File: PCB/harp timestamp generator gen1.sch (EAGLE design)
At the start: 11 parts, among them IC1 ATXMEGAxxxA4U-AU

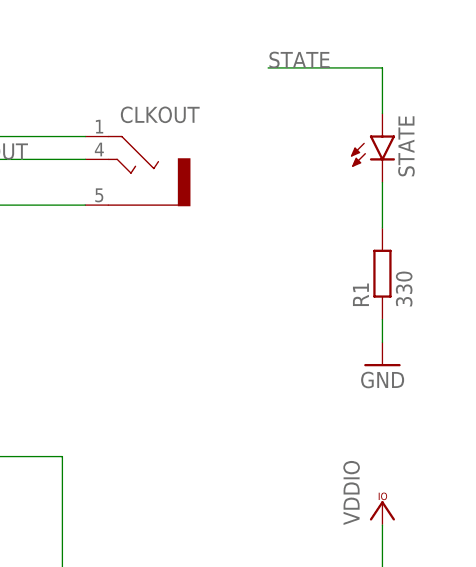
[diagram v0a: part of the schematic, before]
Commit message: Updated R1 to 910 ohms.
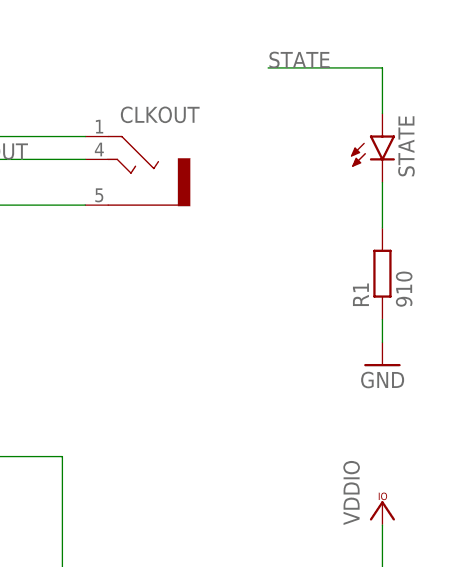
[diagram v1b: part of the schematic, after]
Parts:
- R1: value 330 -> 910
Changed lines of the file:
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@@
 <part name="VCC1" library="supply1" deviceset="VCCIO" device="" value="VDDIO"/>
 <part name="STATE" library="led" library_urn="urn:adsk.eagle:library:259" deviceset="LED" device="CHIP-LED0603" package3d_urn="urn:adsk.eagle:package:15819/3"/>
-<part name="R1" library="rcl" library_urn="urn:adsk.eagle:library:334" deviceset="R-EU_" device="R0402" package3d_urn="urn:adsk.eagle:package:23547/3" value="330"/>
+<part name="R1" library="rcl" library_urn="urn:adsk.eagle:library:334" deviceset="R-EU_" device="R0402" package3d_urn="urn:adsk.eagle:package:23547/3" value="910"/>
 <part name="GND1" library="supply1" deviceset="GND" device=""/>
 <part name="VCC2" library="supply1" deviceset="VCCIO" device="" value="VDDIO"/>

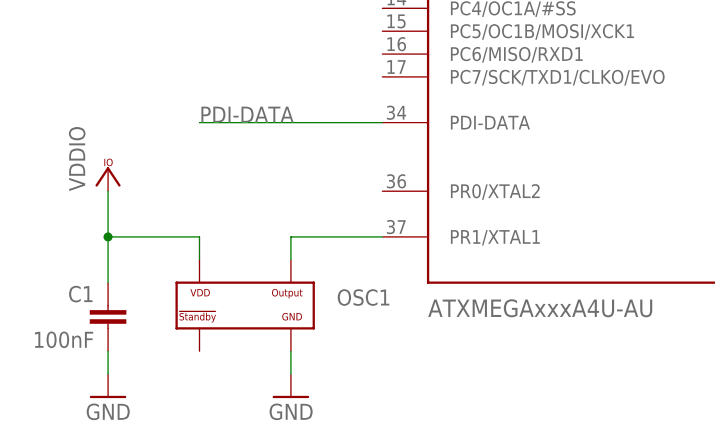
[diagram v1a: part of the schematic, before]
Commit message: Re-designed oscillator footprint for easier manual assembly
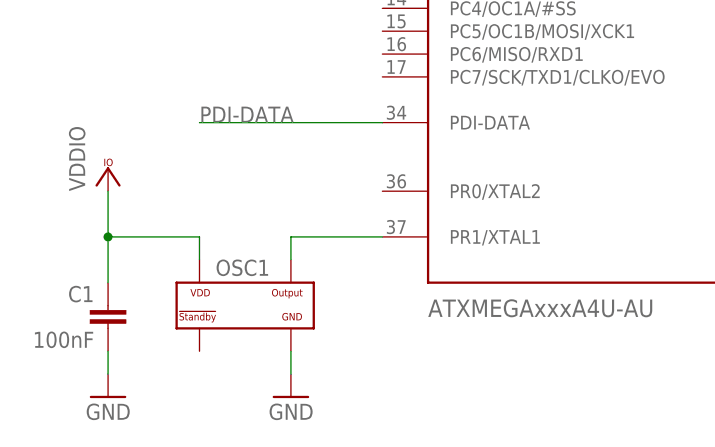
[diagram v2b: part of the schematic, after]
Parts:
- OSC1: value OSCILLATOR -> CNP-MISCELLANEOUS_OSCILLATOR; device CNP-miscellaneous:OSCILLATOR -> harp rfid reader v1.0:CNP-MISCELLANEOUS_OSCILLATOR
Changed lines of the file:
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@@
 <layer number="59" name="tCarbon" color="7" fill="1" visible="no" active="no"/>
 <layer number="60" name="bCarbon" color="7" fill="1" visible="no" active="no"/>
+<layer number="88" name="SimResults" color="9" fill="1" visible="yes" active="yes"/>
+<layer number="89" name="SimProbes" color="9" fill="1" visible="yes" active="yes"/>
 <layer number="90" name="Modules" color="7" fill="1" visible="yes" active="yes"/>
 <layer number="91" name="Nets" color="2" fill="1" visible="yes" active="yes"/>
@@
 <part name="VCC6" library="supply1" deviceset="VCCIO" device="" value="VDDIO"/>
 <part name="FRAME4" library="frames" deviceset="A3L-LOC" device=""/>
-<part name="OSC1" library="CNP-miscellaneous" deviceset="OSCILLATOR" device="" value=""/>
 <part name="GND59" library="supply1" deviceset="GND" device=""/>
 <part name="C1" library="rcl" deviceset="C-EU" device="C0402" value="100nF"/>
@@
 <part name="GND1" library="supply1" deviceset="GND" device=""/>
 <part name="VCC2" library="supply1" deviceset="VCCIO" device="" value="VDDIO"/>
+<part name="OSC1" library="harp rfid reader v1.0" deviceset="CNP-MISCELLANEOUS_OSCILLATOR" device=""/>
 </parts>
 <sheets>
@@
 <attribute name="SHEET" x="357.505" y="5.08" size="2.54" layer="94" font="vector"/>
 </instance>
-<instance part="OSC1" gate="G$1" x="129.54" y="93.98" smashed="yes">
-<attribute name="VALUE" x="139.7" y="91.44" size="1.778" layer="96"/>
-<attribute name="NAME" x="139.7" y="93.98" size="1.778" layer="95"/>
-</instance>
 <instance part="GND59" gate="1" x="134.62" y="83.82" smashed="yes" rot="MR0">
 <attribute name="VALUE" x="137.16" y="81.28" size="1.778" layer="96" rot="MR0"/>
@@
 <instance part="VCC2" gate="G$1" x="226.06" y="137.16" smashed="yes">
 <attribute name="VALUE" x="223.52" y="134.62" size="1.778" layer="96" rot="R90"/>
+</instance>
+<instance part="OSC1" gate="G$1" x="129.54" y="93.98" smashed="yes">
+<attribute name="NAME" x="126.238" y="97.282" size="1.778" layer="95"/>
 </instance>
 </instances>
@@
 </segment>
 <segment>
-<pinref part="OSC1" gate="G$1" pin="VDD"/>
 <wire x1="124.46" y1="99.06" x2="124.46" y2="101.6" width="0.1524" layer="91"/>
 <wire x1="124.46" y1="101.6" x2="114.3" y2="101.6" width="0.1524" layer="91"/>
@@
 <junction x="114.3" y="101.6"/>
 <pinref part="VCC10" gate="G$1" pin="VCCIO"/>
+<pinref part="OSC1" gate="G$1" pin="VDD"/>
 </segment>
 <segment>
@@
 <net name="GND" class="0">
 <segment>
-<pinref part="OSC1" gate="G$1" pin="GND"/>
 <pinref part="GND59" gate="1" pin="GND"/>
 <wire x1="134.62" y1="86.36" x2="134.62" y2="88.9" width="0.1524" layer="91"/>
+<pinref part="OSC1" gate="G$1" pin="GND"/>
 </segment>
 <segment>
@@
 <net name="OSC1" class="0">
 <segment>
-<pinref part="OSC1" gate="G$1" pin="OUTPUT"/>
 <wire x1="134.62" y1="99.06" x2="134.62" y2="101.6" width="0.1524" layer="91"/>
 <pinref part="IC1" gate="G$1" pin="PR1/XTAL1"/>
 <wire x1="134.62" y1="101.6" x2="144.78" y2="101.6" width="0.1524" layer="91"/>
-</segment>
-</net>
+<pinref part="OSC1" gate="G$1" pin="OUTPUT"/>
+</segment>
+</net>
